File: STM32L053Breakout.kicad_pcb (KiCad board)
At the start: 2 copper layers, 69.2 x 67 mm, 59 parts, among them J1 USB_B_Micro, J2 Conn_Coaxial, J3 Male Pinheader 1x20, J4 Male Pinheader 1x20, J5 ARM 10pin, SW1 SW_Push, SW2 SW_Push, SW3 SW_Push, SW4 BOOT0_Switch, SW5 Reset_Switch, U1 RFM95W-868S2, U2 AMS1117-3.3, U3 L80-R, U4 STM32L053R8T6, Y1 Crystal_GND24

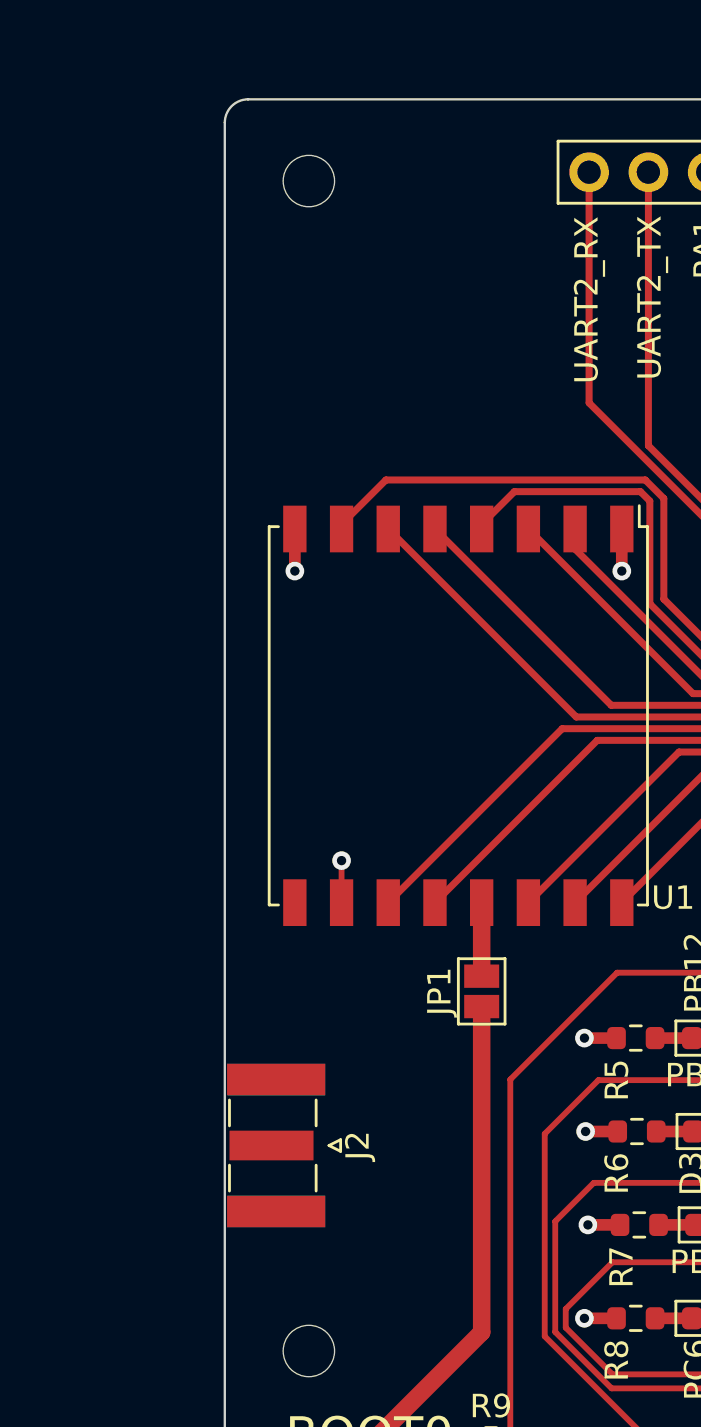
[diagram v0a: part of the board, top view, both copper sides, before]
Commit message: add rfm signal out to CPW & add Logos
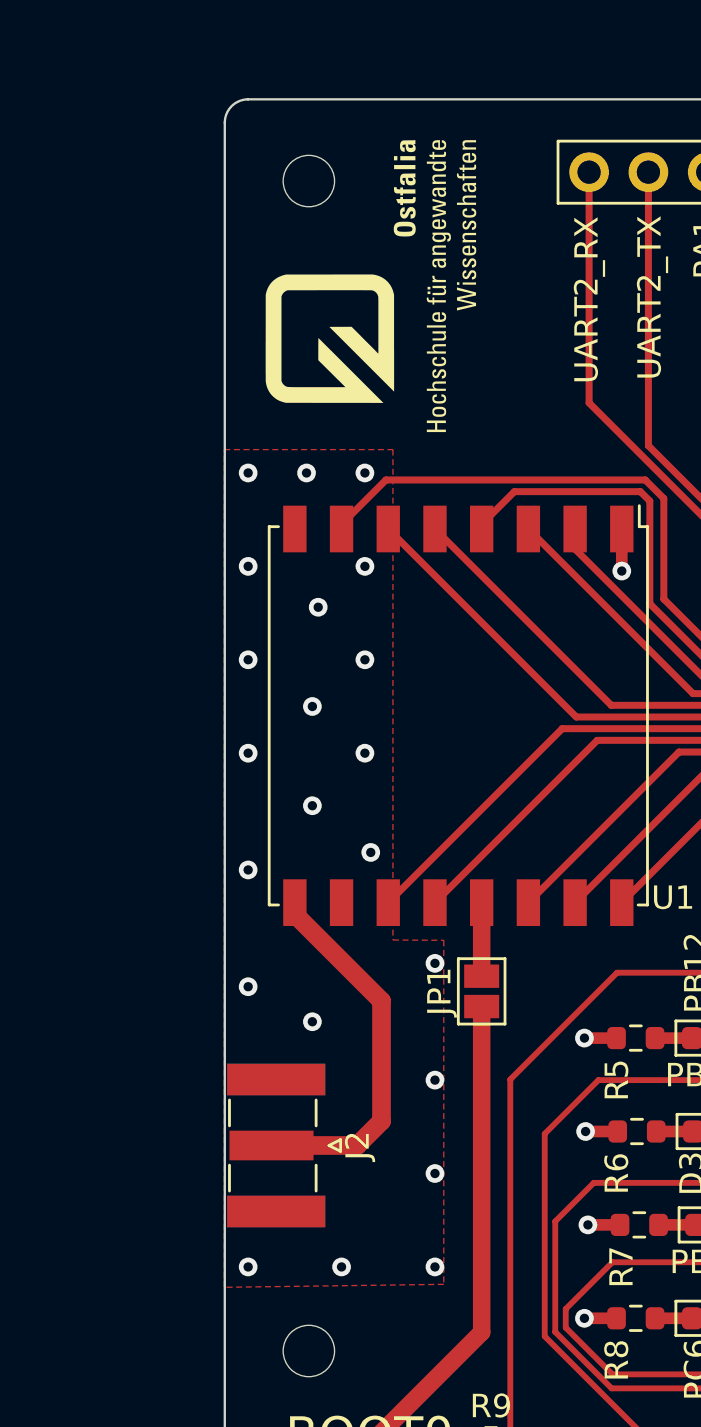
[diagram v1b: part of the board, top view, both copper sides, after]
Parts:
- added  : LOGO, Logo:ostfalia_logo_5.5mm, F.Cu at (90.5, 78.2)
- added  : LOGO, Logo:ostfalia_logo_schrift_12.5mm, F.Cu at (95.0, 76.0)
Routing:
- net Net-(J2-Pad1): track 0.00 -> 16.0 mm
- net GND: track 76.9 -> 73.3 mm, vias 30 -> 50
- added copper zone on F.Cu, net GND

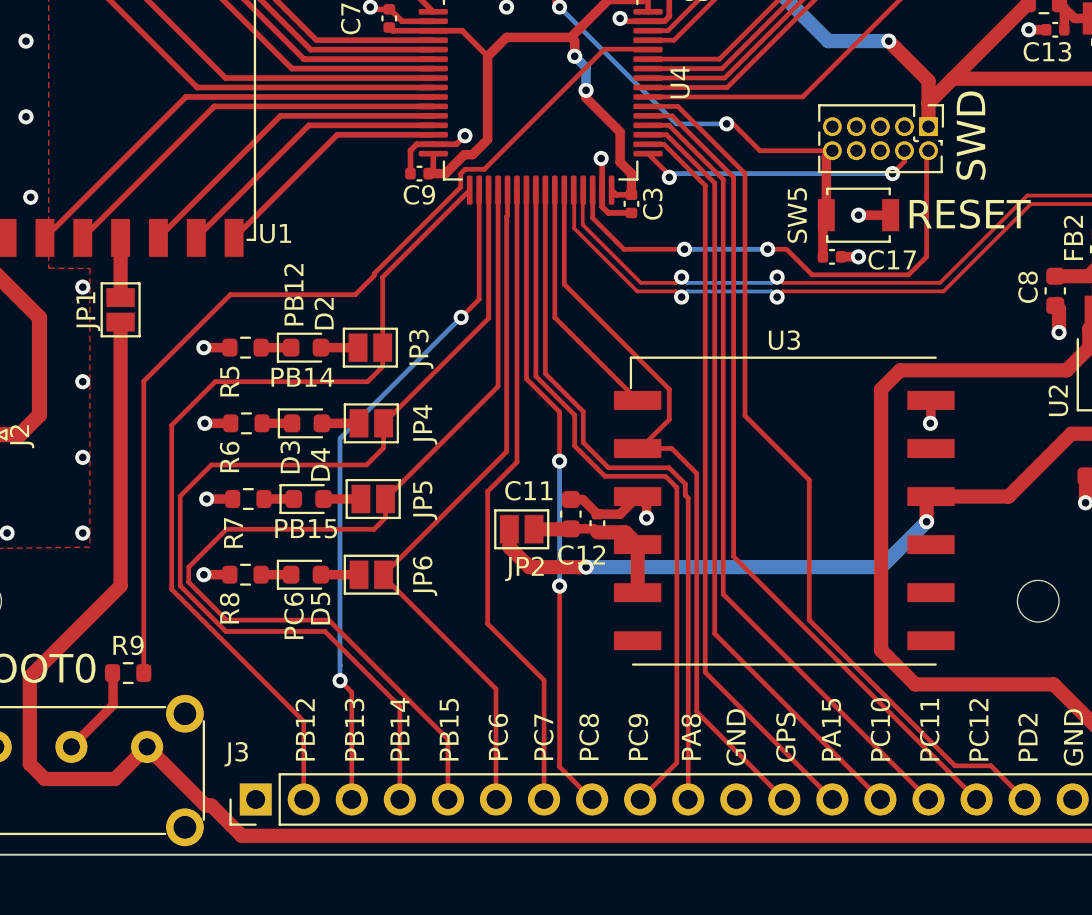
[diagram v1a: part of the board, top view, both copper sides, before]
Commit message: Change Keepout and add 3.3V Rail to RFM
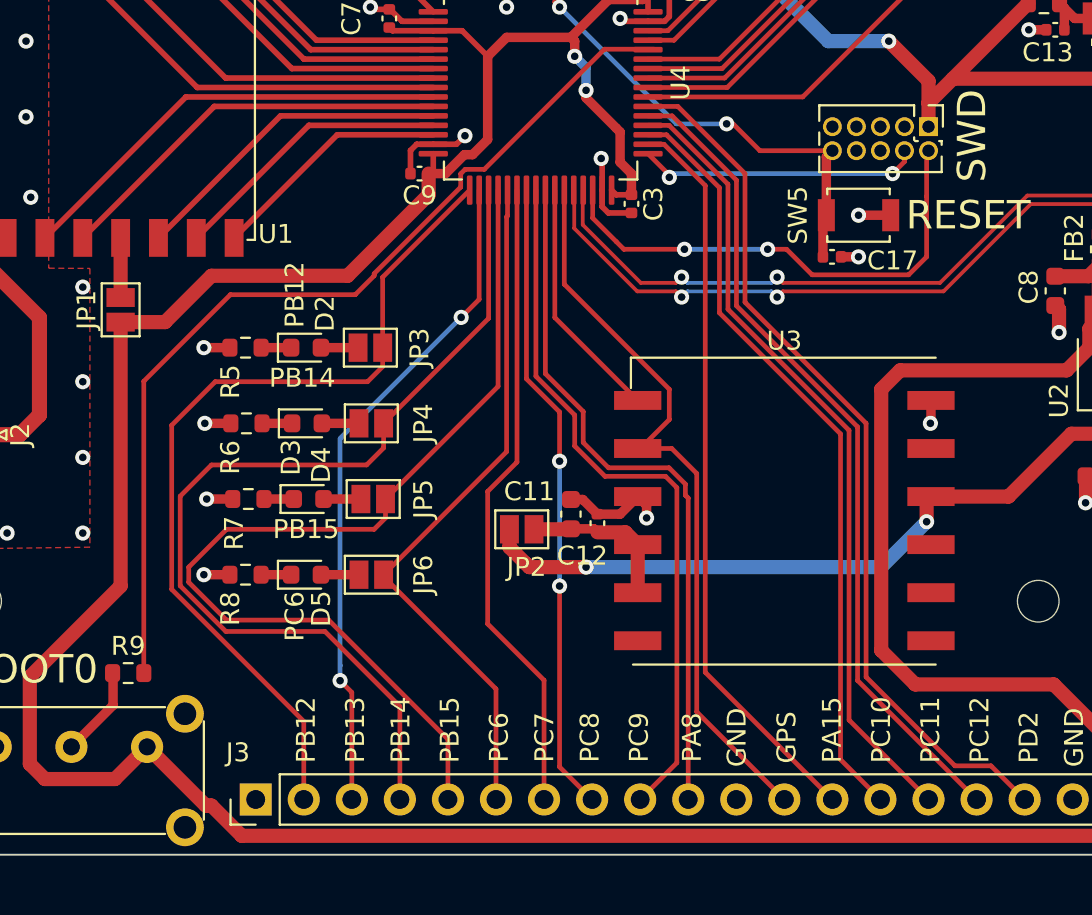
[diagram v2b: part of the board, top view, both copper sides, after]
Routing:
- net +3.3V: track 330.7 -> 350.9 mm
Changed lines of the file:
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@@
   (segment (start 117.55 118.75) (end 118.4 119.6) (width 0.75) (layer "F.Cu") (net 1))
   (segment (start 112.4 81.4) (end 112.6 81.2) (width 0.75) (layer "F.Cu") (net 1))
+  (segment (start 99.35 106.85) (end 101.8 104.4) (width 0.75) (layer "F.Cu") (net 1))
   (segment (start 147.25 112.75) (end 151 112.75) (width 0.75) (layer "F.Cu") (net 1))
   (segment (start 152.25 103.35) (end 152.25 96.85) (width 0.75) (layer "F.Cu") (net 1))
@@
   (segment (start 120.8 91.8) (end 122.8 89.8) (width 0.5) (layer "F.Cu") (net 1))
   (segment (start 152 80.8) (end 152.725 81.525) (width 0.75) (layer "F.Cu") (net 1))
+  (segment (start 101.8 104.4) (end 109 104.4) (width 0.75) (layer "F.Cu") (net 1))
   (segment (start 118.6 119.8) (end 121.6 119.8) (width 0.75) (layer "F.Cu") (net 1))
   (segment (start 150.4 134) (end 149.86 133.46) (width 0.75) (layer "F.Cu") (net 1))
@@
   (segment (start 113.525 91.45) (end 115.05 91.45) (width 0.3) (layer "F.Cu") (net 1))
   (segment (start 124 100.12) (end 123.195 100.12) (width 0.3) (layer "F.Cu") (net 1))
+  (segment (start 109 104.4) (end 113.28 100.12) (width 0.75) (layer "F.Cu") (net 1))
+  (segment (start 97 106.85) (end 99.35 106.85) (width 0.75) (layer "F.Cu") (net 1))
   (segment (start 153.8 115.0125) (end 153.2625 115.0125) (width 0.75) (layer "F.Cu") (net 1))
   (segment (start 124 100.12) (end 124 99) (width 0.5) (layer "F.Cu") (net 1))
@@
   (segment (start 150.4 134) (end 103.4 134) (width 0.75) (layer "F.Cu") (net 1))
   (segment (start 129.2 86.8) (end 128.8 86.4) (width 0.75) (layer "F.Cu") (net 1))
+  (segment (start 113.28 100.12) (end 113.28 99) (width 0.75) (layer "F.Cu") (net 1))
   (segment (start 150.9 95.5) (end 149.385 93.985) (width 0.75) (layer "F.Cu") (net 1))
   (segment (start 137.6 92) (end 139.7 94.1) (width 0.75) (layer "F.Cu") (net 1))
@@
   (segment (start 134.62 132.08) (end 127.9 125.36) (width 0.25) (layer "F.Cu") (net 34))
   (segment (start 125.715685 97.45) (end 124.875 97.45) (width 0.25) (layer "F.Cu") (net 34))
+  (segment (start 128.65 99.747919) (end 128.65 106.359188) (width 0.25) (layer "F.Cu") (net 35))
+  (segment (start 125.852081 96.95) (end 128.65 99.747919) (width 0.25) (layer "F.Cu") (net 35))
   (segment (start 124.875 96.95) (end 125.852081 96.95) (width 0.25) (layer "F.Cu") (net 35))
-  (segment (start 125.852081 96.95) (end 128.4 99.497919) (width 0.25) (layer "F.Cu") (net 35))
-  (segment (start 128.4 123.32) (end 137.16 132.08) (width 0.25) (layer "F.Cu") (net 35))
-  (segment (start 128.4 99.497919) (end 128.4 123.32) (width 0.25) (layer "F.Cu") (net 35))
-  (segment (start 128.85 121.23) (end 139.7 132.08) (width 0.25) (layer "F.Cu") (net 36))
+  (segment (start 128.65 106.359188) (end 135.05 112.759188) (width 0.25) (layer "F.Cu") (net 35))
+  (segment (start 135.05 112.759188) (end 135.05 129.97) (width 0.25) (layer "F.Cu") (net 35))
+  (segment (start 135.05 129.97) (end 137.16 132.08) (width 0.25) (layer "F.Cu") (net 35))
+  (segment (start 135.5 127.88) (end 139.7 132.08) (width 0.25) (layer "F.Cu") (net 36))
+  (segment (start 135.5 112.572792) (end 135.5 127.88) (width 0.25) (layer "F.Cu") (net 36))
+  (segment (start 125.988477 96.45) (end 129.1 99.561523) (width 0.25) (layer "F.Cu") (net 36))
   (segment (start 124.875 96.45) (end 125.988477 96.45) (width 0.25) (layer "F.Cu") (net 36))
-  (segment (start 128.85 99.311523) (end 128.85 121.23) (width 0.25) (layer "F.Cu") (net 36))
-  (segment (start 125.988477 96.45) (end 128.85 99.311523) (width 0.25) (layer "F.Cu") (net 36))
-  (segment (start 126.15 95.95) (end 129.4 99.2) (width 0.25) (layer "F.Cu") (net 37))
-  (segment (start 129.4 99.2) (end 129.4 119.24) (width 0.25) (layer "F.Cu") (net 37))
+  (segment (start 129.1 99.561523) (end 129.1 106.172792) (width 0.25) (layer "F.Cu") (net 36))
+  (segment (start 129.1 106.172792) (end 135.5 112.572792) (width 0.25) (layer "F.Cu") (net 36))
+  (segment (start 135.95 125.79) (end 142.24 132.08) (width 0.25) (layer "F.Cu") (net 37))
+  (segment (start 135.95 112.386396) (end 135.95 125.79) (width 0.25) (layer "F.Cu") (net 37))
+  (segment (start 129.55 105.986396) (end 135.95 112.386396) (width 0.25) (layer "F.Cu") (net 37))
+  (segment (start 126.15 95.95) (end 129.55 99.35) (width 0.25) (layer "F.Cu") (net 37))
   (segment (start 124.875 95.95) (end 126.15 95.95) (width 0.25) (layer "F.Cu") (net 37))
-  (segment (start 129.4 119.24) (end 142.24 132.08) (width 0.25) (layer "F.Cu") (net 37))
-  (segment (start 133.4 122.603604) (end 133.4 115.2) (width 0.25) (layer "F.Cu") (net 38))
-  (segment (start 130 99) (end 126.45 95.45) (width 0.25) (layer "F.Cu") (net 38))
+  (segment (start 129.55 99.35) (end 129.55 105.986396) (width 0.25) (layer "F.Cu") (net 37))
   (segment (start 126.45 95.45) (end 124.875 95.45) (width 0.25) (layer "F.Cu") (net 38))
-  (segment (start 130 111.8) (end 130 99) (width 0.25) (layer "F.Cu") (net 38))
+  (segment (start 136.4 125.603604) (end 136.4 112.2) (width 0.25) (layer "F.Cu") (net 38))
   (segment (start 144.78 132.08) (end 143.001802 130.301802) (width 0.25) (layer "F.Cu") (net 38))
   (segment (start 143.001802 130.301802) (end 141.098198 130.301802) (width 0.25) (layer "F.Cu") (net 38))
-  (segment (start 141.098198 130.301802) (end 133.4 122.603604) (width 0.25) (layer "F.Cu") (net 38))
-  (segment (start 133.4 115.2) (end 130 111.8) (width 0.25) (layer "F.Cu") (net 38))
+  (segment (start 130 99) (end 126.45 95.45) (width 0.25) (layer "F.Cu") (net 38))
+  (segment (start 130 105.8) (end 130 99) (width 0.25) (layer "F.Cu") (net 38))
+  (segment (start 141.098198 130.301802) (end 136.4 125.603604) (width 0.25) (layer "F.Cu") (net 38))
+  (segment (start 136.4 112.2) (end 130 105.8) (width 0.25) (layer "F.Cu") (net 38))
   (segment (start 146.625 90) (end 146.88 90.255) (width 0.5) (layer "F.Cu") (net 39))
   (segment (start 133.05 94.95) (end 139.2 88.8) (width 0.25) (layer "F.Cu") (net 39))

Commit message: Add sensor and change bom for GPS
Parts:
- added C700: 10u, Capacitor_SMD:C_0603_1608Metric, F.Cu at (131.0, 81.0)
- added C701: 100n, Capacitor_SMD:C_0402_1005Metric, F.Cu at (133.8, 81.8)
- added C702: 100n, Capacitor_SMD:C_0402_1005Metric, F.Cu at (133.8, 80.6)
- added JP700: SolderJumper_2_Open, Jumper:SolderJumper-2_P1.3mm_Open_Pad1.0x1.5mm, F.Cu at (129.4, 83.2)
- added U700: LIS2HH12, Package_LGA:LGA-12_2x2mm_P0.5mm, F.Cu at (133.4, 84.0)
- moved H4 4.37 mm to (140.2, 80.8)
- renumbered C8 to C100, C10 to C101, C1 to C200, C3 to C201, C5 to C202, C7 to C203, C9 to C204, C2 to C205, C4 to C206, C6 to C207, C13 to C400, C14 to C401, C15 to C402, C17 to C500, C16 to C501, C18 to C502, C11 to C800, C12 to C801, D1 to D100, D2 to D400, D3 to D401, D4 to D402, D5 to D403, FB2 to FB100, FB1 to FB200, J1 to J100, J3 to J300, J4 to J301, J2 to J600, JP3 to JP400, JP4 to JP401, JP5 to JP402, JP6 to JP403, JP1 to JP600, JP2 to JP800, R1 to R100, R5 to R400, R6 to R401, R7 to R402, R8 to R403, R2 to R404, R3 to R405, R4 to R406, R9 to R500, SW1 to SW400, SW2 to SW401, SW3 to SW402, SW5 to SW500, SW4 to SW501, U2 to U100, U4 to U500, U1 to U600, U3 to U800, Y1 to Y500
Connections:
- net PB6 renamed I2C1_SCL
- net PB7 renamed I2C1_SDA
- J301 pad 7: PB8 -> unconnected-(J301-Pad7)
- J301 pad 8: PB9 -> unconnected-(J301-Pad8)
- U500 pad 61: PB8 -> INT1
- U500 pad 62: PB9 -> INT2
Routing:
- net PB8: track 25.7 -> 0.00 mm
- net PB9: track 23.9 -> 0.00 mm
- net INT1: track 0.00 -> 12.3 mm
- net INT2: track 0.00 -> 12.0 mm
- net +3.3V: track 350.9 -> 362.5 mm
- net GND: track 73.3 -> 83.7 mm, vias 50 -> 51
- net I2C1_SCL: track 30.8 -> 40.7 mm
- net PB4: track 36.5 -> 30.9 mm
- net Net-(JP700-Pad2): track 0.00 -> 4.64 mm
- net PB5: track 40.4 -> 35.9 mm
- net I2C1_SDA: track 29.1 -> 30.7 mm, vias 0 -> 2

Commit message: Add Rev Number
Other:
- board text added: "Rev 1.0"
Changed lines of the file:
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@@
     (effects (font (size 1 1) (thickness 0.15)))
+  )
+  (gr_text "Rev 1.0" (at 97.6 71.6 90) (layer "F.SilkS")
+    (effects (font (size 0.7 0.7) (thickness 0.1)))
   )
   (gr_text "3.3V" (at 150 74.6 90) (layer "F.SilkS")
